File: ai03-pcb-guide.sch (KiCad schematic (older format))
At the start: 2 parts

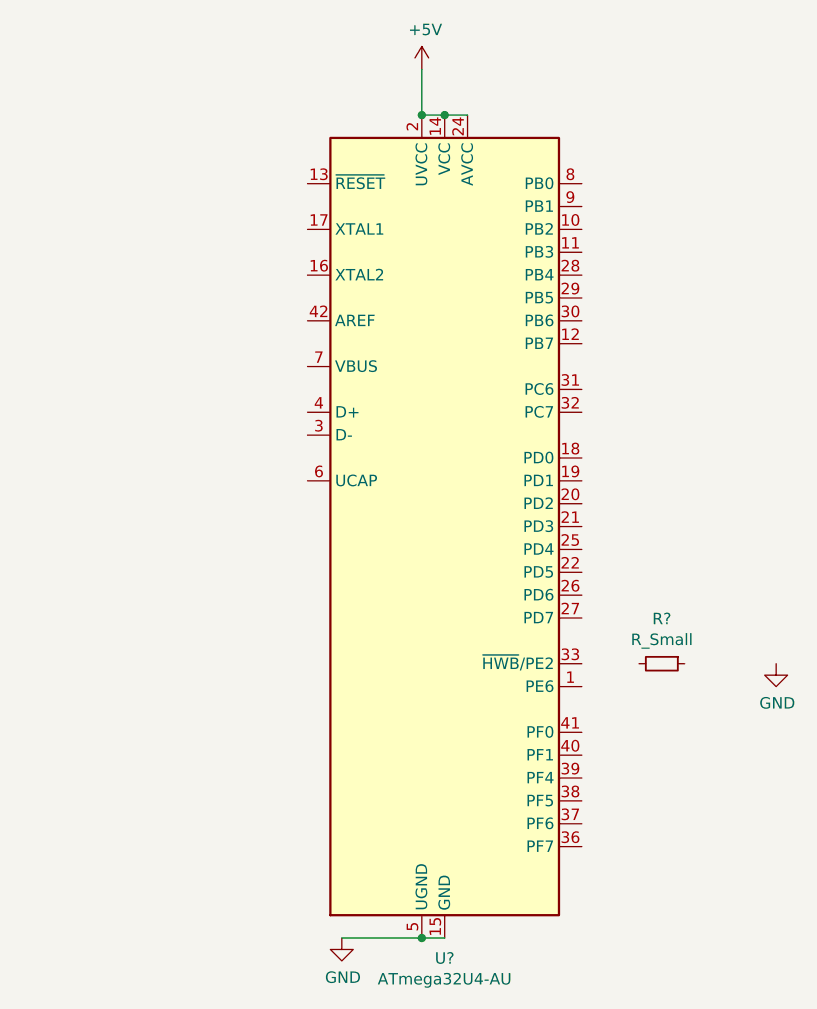
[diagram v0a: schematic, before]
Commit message: added more resisters
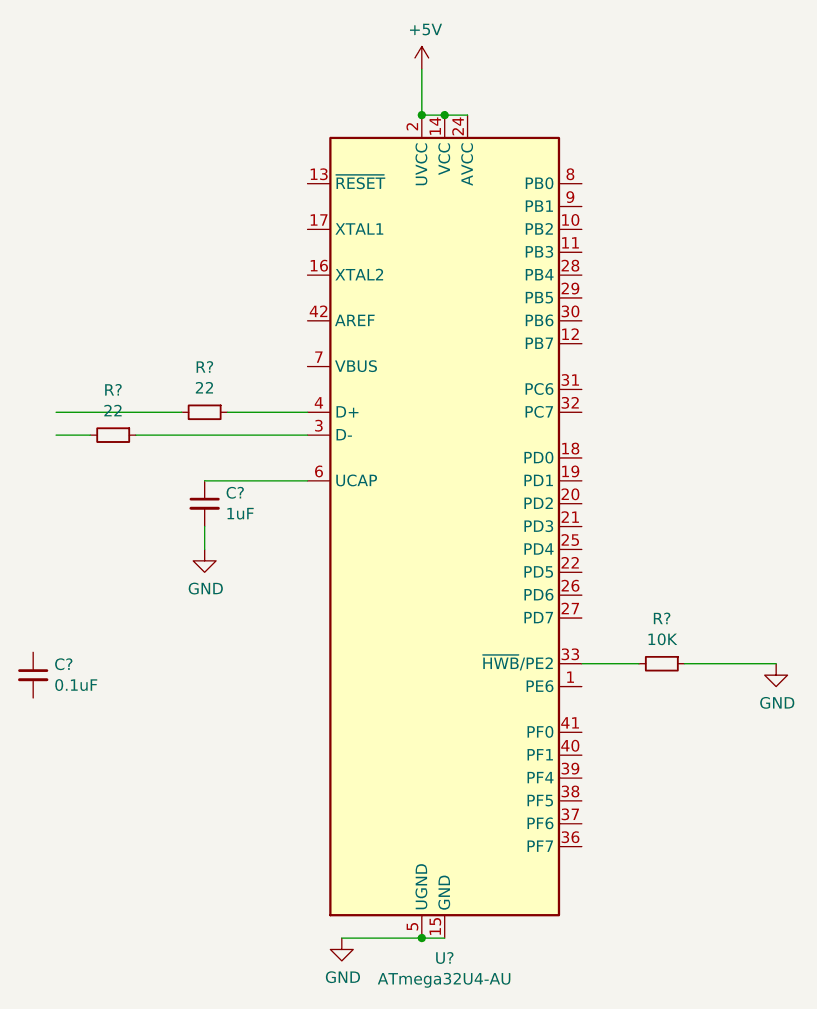
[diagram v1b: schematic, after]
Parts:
- added C?: 1uF, symbol Device:C_Small
- added C?: 0.1uF, symbol Device:C_Small
- added R? (x2): 22, symbol Device:R_Small
- R?: value R_Small -> 10K
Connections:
- wire segments 5 -> 13
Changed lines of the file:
@@
 P 3500 4400
 F 0 "R?" V 3304 4400 50  0000 C CNN
-F 1 "R_Small" V 3395 4400 50  0000 C CNN
+F 1 "10K" V 3395 4400 50  0000 C CNN
 F 2 "" H 3500 4400 50  0001 C CNN
 F 3 "~" H 3500 4400 50  0001 C CNN
@@
 	1    0    0    -1
 $EndComp
+Wire Wire Line
+	3150 4400 3400 4400
+Wire Wire Line
+	3600 4400 4000 4400
+Wire Wire Line
+	1950 3300 1600 3300
+Wire Wire Line
+	1400 3300 850  3300
+Wire Wire Line
+	1000 3400 850  3400
+$Comp
+L Device:R_Small R?
+U 1 1 5EB94895
+P 1100 3400
+F 0 "R?" V 904 3400 50  0000 C CNN
+F 1 "22" V 995 3400 50  0000 C CNN
+F 2 "" H 1100 3400 50  0001 C CNN
+F 3 "~" H 1100 3400 50  0001 C CNN
+	1    1100 3400
+	0    1    1    0
+$EndComp
+Wire Wire Line
+	1950 3400 1200 3400
+$Comp
+L Device:R_Small R?
+U 1 1 5EB93EA8
+P 1500 3300
+F 0 "R?" V 1304 3300 50  0000 C CNN
+F 1 "22" V 1395 3300 50  0000 C CNN
+F 2 "" H 1500 3300 50  0001 C CNN
+F 3 "~" H 1500 3300 50  0001 C CNN
+	1    1500 3300
+	0    1    1    0
+$EndComp
+$Comp
+L Device:C_Small C?
+U 1 1 5EB97218
+P 1500 3700
+F 0 "C?" H 1592 3746 50  0000 L CNN
+F 1 "1uF" H 1592 3655 50  0000 L CNN
+F 2 "" H 1500 3700 50  0001 C CNN
+F 3 "~" H 1500 3700 50  0001 C CNN
+	1    1500 3700
+	1    0    0    -1
+$EndComp
+Wire Wire Line
+	1950 3600 1500 3600
+Wire Wire Line
+	1500 3800 1500 3900
+$Comp
+L power:GND #PWR?
+U 1 1 5EB983E5
+P 1500 3900
+F 0 "#PWR?" H 1500 3650 50  0001 C CNN
+F 1 "GND" H 1505 3727 50  0000 C CNN
+F 2 "" H 1500 3900 50  0001 C CNN
+F 3 "" H 1500 3900 50  0001 C CNN
+	1    1500 3900
+	1    0    0    -1
+$EndComp
+$Comp
+L Device:C_Small C?
+U 1 1 5EB997CF
+P 750 4450
+F 0 "C?" H 842 4496 50  0000 L CNN
+F 1 "0.1uF" H 842 4405 50  0000 L CNN
+F 2 "" H 750 4450 50  0001 C CNN
+F 3 "~" H 750 4450 50  0001 C CNN
+	1    750  4450
+	1    0    0    -1
+$EndComp
